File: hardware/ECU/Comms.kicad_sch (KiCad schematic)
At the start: 4 parts, among them J1 Conn_01x04, U17 W25Q32JVSS, U3 74AHC1G32, U4 ADXL343

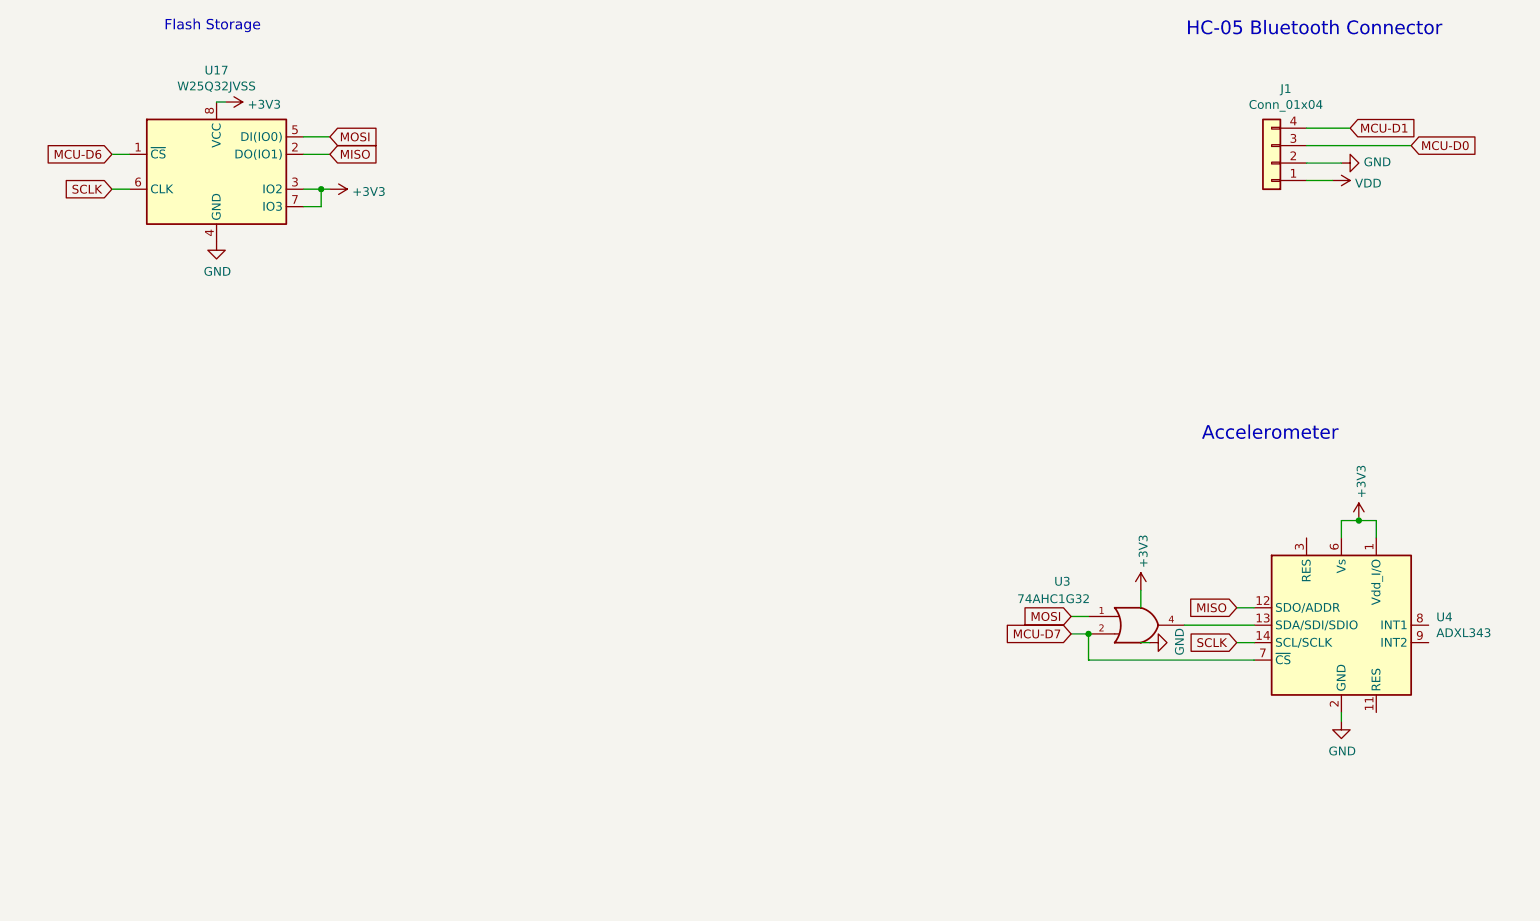
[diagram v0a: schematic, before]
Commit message: Replace speeduino submodule with HasiKe fork, fix teensy.pretty path
- Switch speeduino from speeduino/speeduino to HasiKe/speeduino
- Fix teensy.pretty submodule path case mismatch (Hardware -> hardware)
- Add ISL9V5036P3-F085 component library
- Various ECU schematic updates
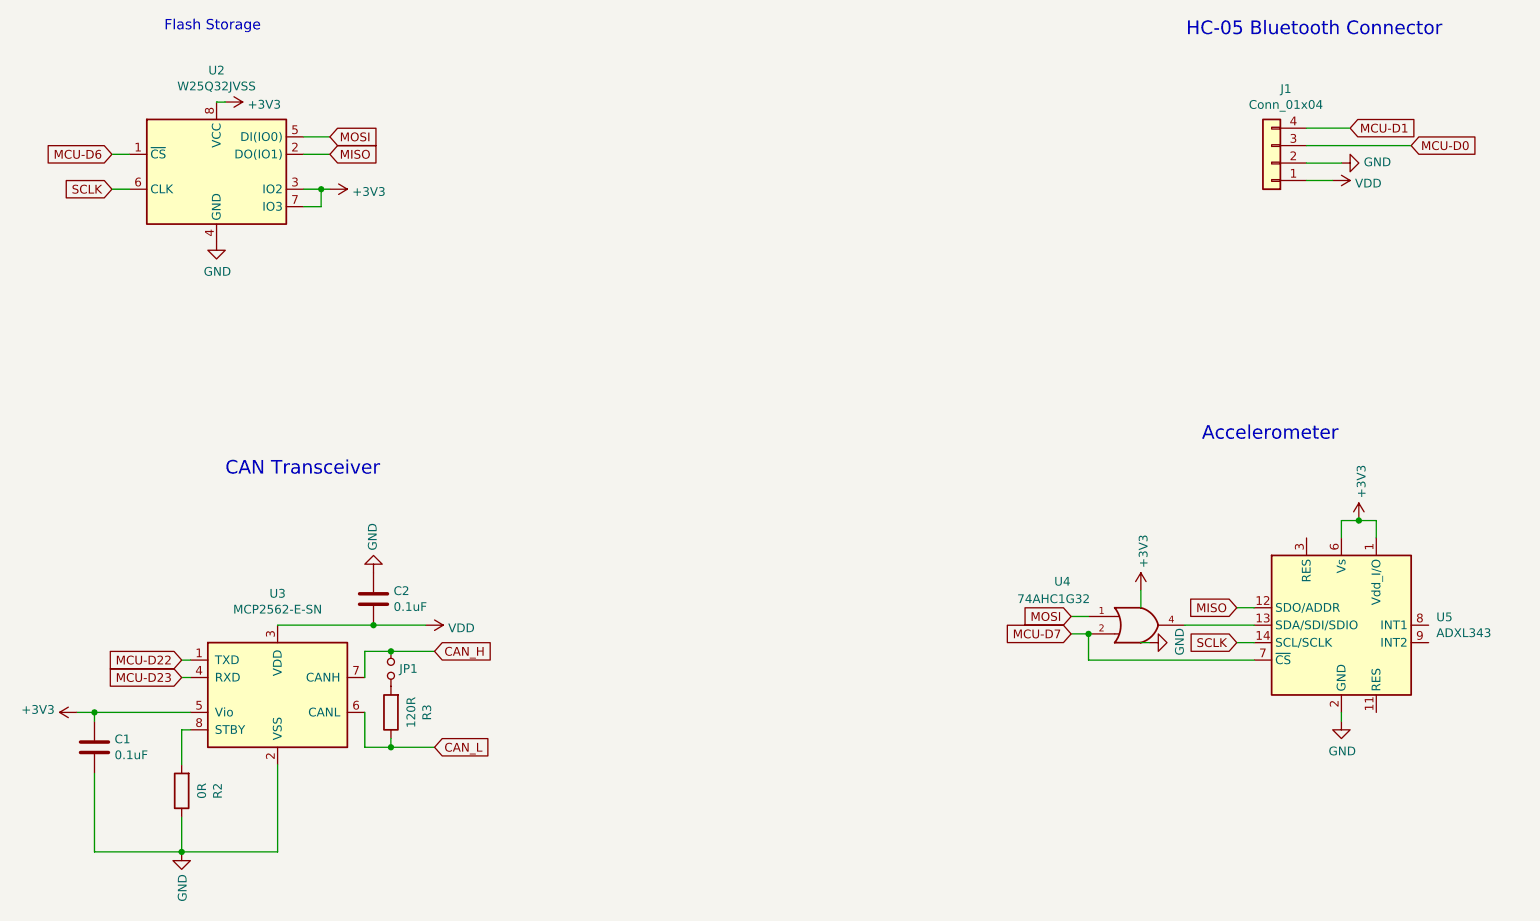
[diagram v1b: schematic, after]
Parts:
- added C1, C2: 0.1uF, Capacitor_SMD:C_0805_2012Metric, symbol Device:C
- added JP1: Jumper_NO_Small, Jumper:SolderJumper-2_P1.3mm_Open_Pad1.0x1.5mm, symbol Device:Jumper_NO_Small
- added R2: 0R, Resistor_SMD:R_0805_2012Metric, symbol Device:R
- added R3: 120R, Resistor_SMD:R_0805_2012Metric, symbol Device:R
- added U3: MCP2562-E-SN, Package_SO:SOIC-8_3.9x4.9mm_P1.27mm, symbol Interface_CAN_LIN:MCP2562-E-SN
- renumbered U17 to U2, U3 to U4, U4 to U5
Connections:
- net +3V3: now also C1.1, U3.5 (Vio)
- net GND: now also C1.2, C2.1, R2.1, U3.2 (VSS)
- net VDD: now also C2.2, U3.3 (VDD)
- new net: R2.2, U3.8 (STBY)
- new net: JP1.2, R3.2
- new net CAN_H: JP1.1, U3.7 (CANH)
- new net CAN_L: R3.1, U3.6 (CANL)
- new net MCU-D22: U3.1 (TXD)
- new net MCU-D23: U3.4 (RXD)
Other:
- note added: "CAN Transceiver"
